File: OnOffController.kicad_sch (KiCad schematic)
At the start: 33 parts, among them J1 S2B-PH-K-SLFSN, J2 Conn_01x02_Pin, J3 Conn_01x04_Pin, J4 Conn_01x04_Pin, J8 47589-0001, SW1 KMR211GLFS, U1 STM6601, U2 MCP73831-2-OT, U3 SPX3819M5-L

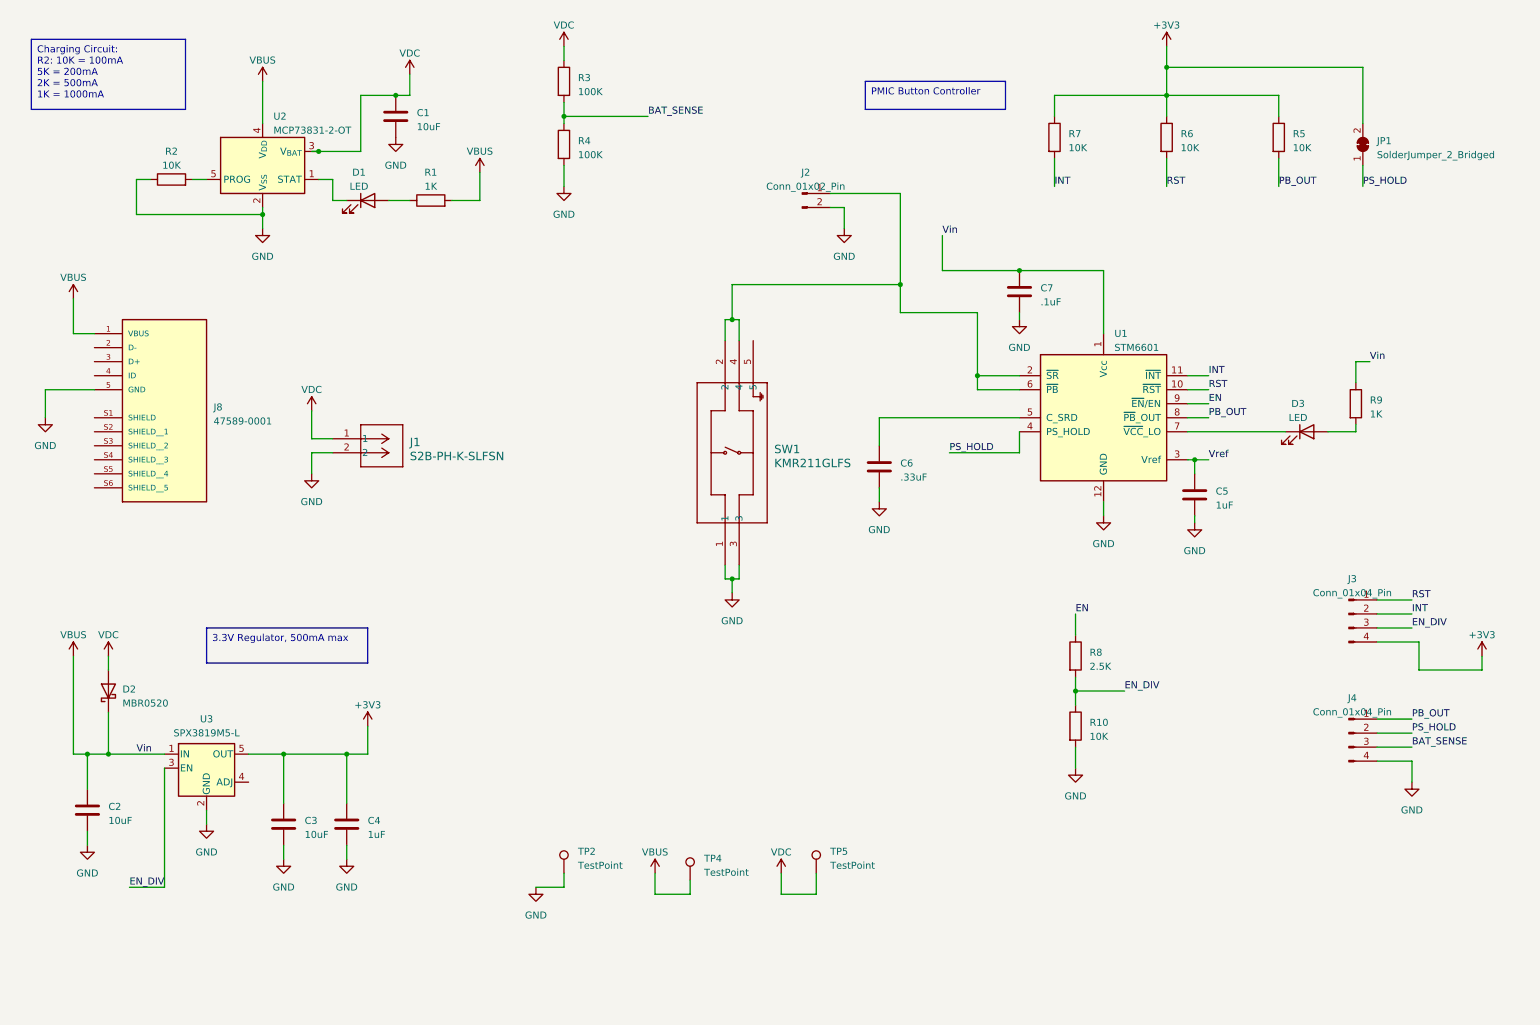
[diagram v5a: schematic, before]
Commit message: Updated all parts to smaller package sizes and found cheaper alternatives
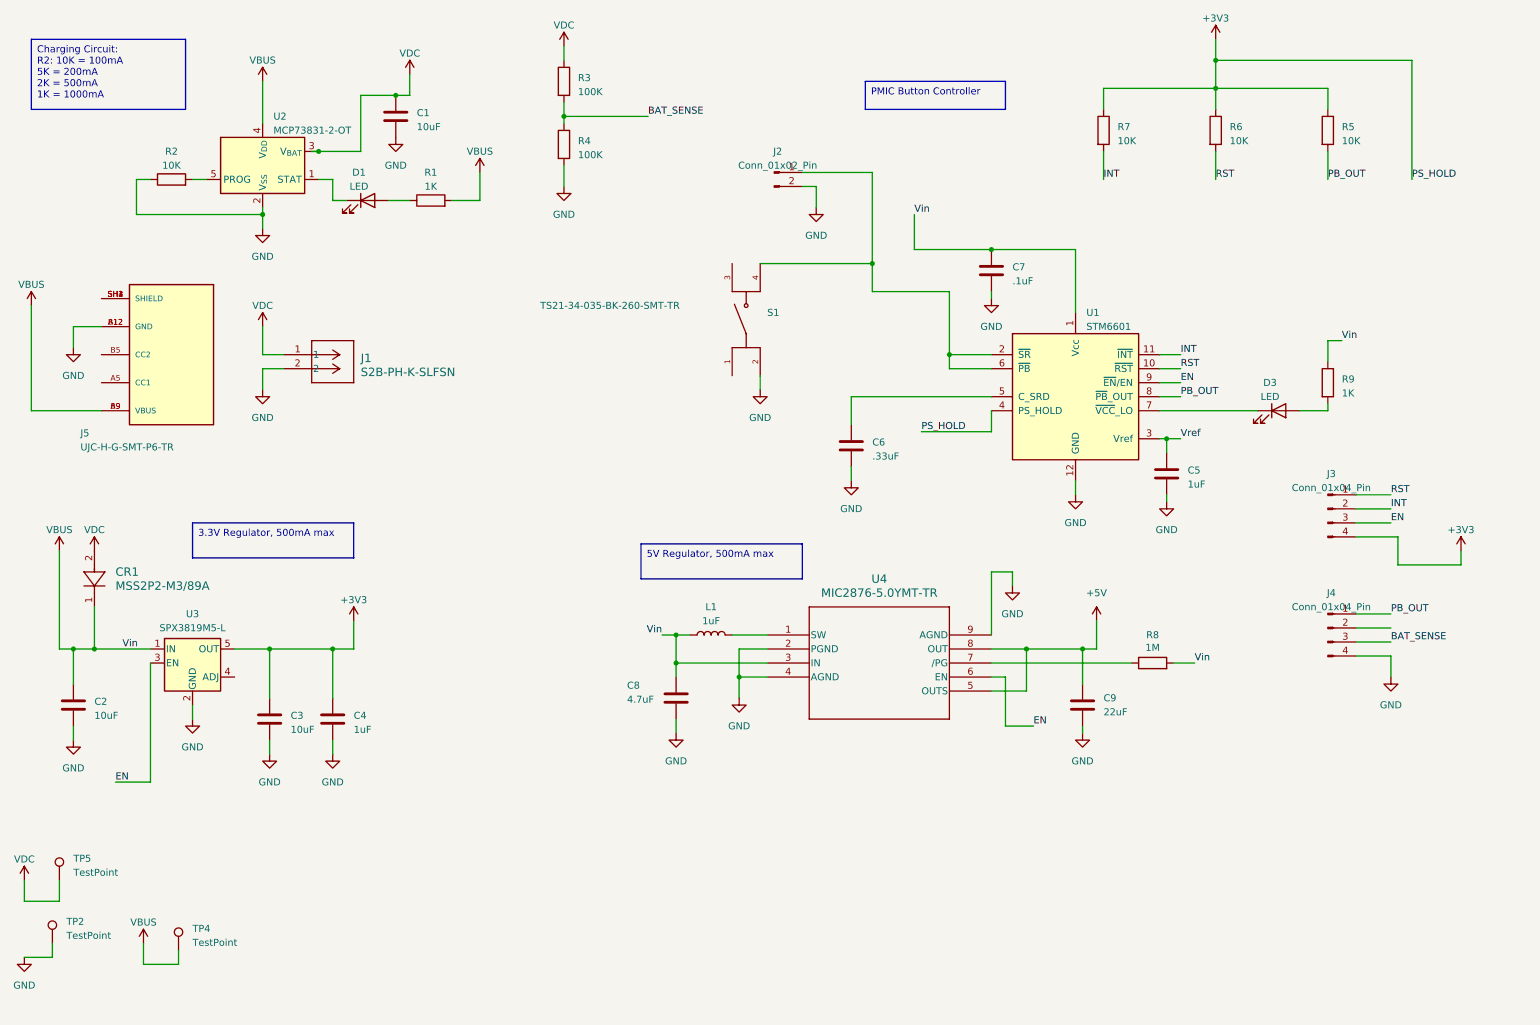
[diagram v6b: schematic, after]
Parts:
- removed D2: MBR0520, Diode_SMD:D_SOD-123, symbol Diode:MBR0520
- removed J8: 47589-0001, 47589_0001_USB_B:MOLEX_47589-0001, symbol 47589-0001_MOLEX_USB_B:47589-0001
- removed JP1: SolderJumper_2_Bridged, Jumper:SolderJumper-2_P1.3mm_Bridged_Pad1.0x1.5mm, symbol Jumper:SolderJumper_2_Bridged
- removed R10: 10K, Resistor_SMD:R_0603_1608Metric_Pad0.98x0.95mm_HandSolder, symbol Device:R
- removed SW1: KMR211GLFS, KMR2_Switch:KMR2xxG_CNK, symbol 2024-04-06_17-09-25_KMR_Switch:KMR211GLFS
- added C8: 4.7uF, Capacitor_SMD:C_0402_1005Metric, symbol Device:C
- added C9: 22uF, Capacitor_SMD:C_0603_1608Metric, symbol Device:C
- added CR1: MSS2P2-M3/89A, MSS2P2-M3:DIODE_MSP3V3, symbol MSS2P2-M3:MSS2P2-M3_89A
- added J5: UJC-H-G-SMT-P6-TR, UJC-H-G-SMT-P6-TR:SAMESKY_UJC-H-G-SMT-P6-TR, symbol UJC-H-G-SMT-P6-TR:UJC-H-G-SMT-P6-TR
- added L1: 1uF, Inductor_SMD:L_0805_2012Metric, symbol Device:L
- added S1: TS21-34-035-BK-260-SMT-TR, TS21-34-035-BK-260-SMT-TR:SW_TS21-34-035-BK-260-SMT-TR, symbol TS21_34_035_BK_260_SMT_TR:TS21-34-035-BK-260-SMT-TR
- added U4: MIC2876-5.0YMT-TR, MIC2876-5:UDFN8_2X2_MCH, symbol MIC2876-5:MIC2876-5.0YMT-TR
- C1, C2, C3, C4, C5, C6, C7: footprint Capacitor_SMD:C_0603_1608Metric_Pad1.08x0.95mm_HandSolder -> Capacitor_SMD:C_0402_1005Metric
- D1: footprint LED_SMD:LED_0805_2012Metric_Pad1.15x1.40mm_HandSolder -> LED_SMD:LED_0603_1608Metric
- D3: footprint LED_SMD:LED_0603_1608Metric_Pad1.05x0.95mm_HandSolder -> LED_SMD:LED_0603_1608Metric
- R1, R2, R3, R4, R5, R6, R7, R9: footprint Resistor_SMD:R_0603_1608Metric_Pad0.98x0.95mm_HandSolder -> Resistor_SMD:R_0402_1005Metric
- R8: value 2.5K -> 1M; footprint Resistor_SMD:R_0603_1608Metric_Pad0.98x0.95mm_HandSolder -> Resistor_SMD:R_0402_1005Metric
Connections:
- net +3V3: now also U1.4 (PS_HOLD)
- net EN: now also J3.3 (Pin_3), U3.3 (EN), U4.6 (EN); no longer R8.1
- net GND: now also C8.2, C9.2, J5.A12 (GND), J5.B12 (GND), S1.2, U4.2 (PGND), U4.4 (AGND), U4.9 (AGND)
- net VBUS: now also R8.2, C8.1, CR1.1, J5.A9 (VBUS), J5.B9 (VBUS), L1.1, U4.3 (IN)
- net VDC: now also CR1.2
- net at J2.1 (Pin_1), U1.2 (~{SR}), U1.6 (~{PB}): now also S1.4
- removed net EN_DIV: J3.3 (Pin_3), R8.2, U3.3 (EN)
- net PS_HOLD: no longer names the net of J4.2 (Pin_2)
- net PS_HOLD: no longer U1.4 (PS_HOLD)
- new net: L1.2, U4.1 (SW)
- new net: R8.1, U4.7 (/PG)
- new net: J5.SH1 (SHIELD), J5.SH2 (SHIELD), J5.SH3 (SHIELD), J5.SH4 (SHIELD)
- new net +5V: C9.1, U4.5 (OUTS), U4.8 (OUT)
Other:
- moved on the sheet: C2, C3, C4, C5, C6, C7, D3, J1, J2, J3, J4, R5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

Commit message: Updated to 5V and 3.3V versions
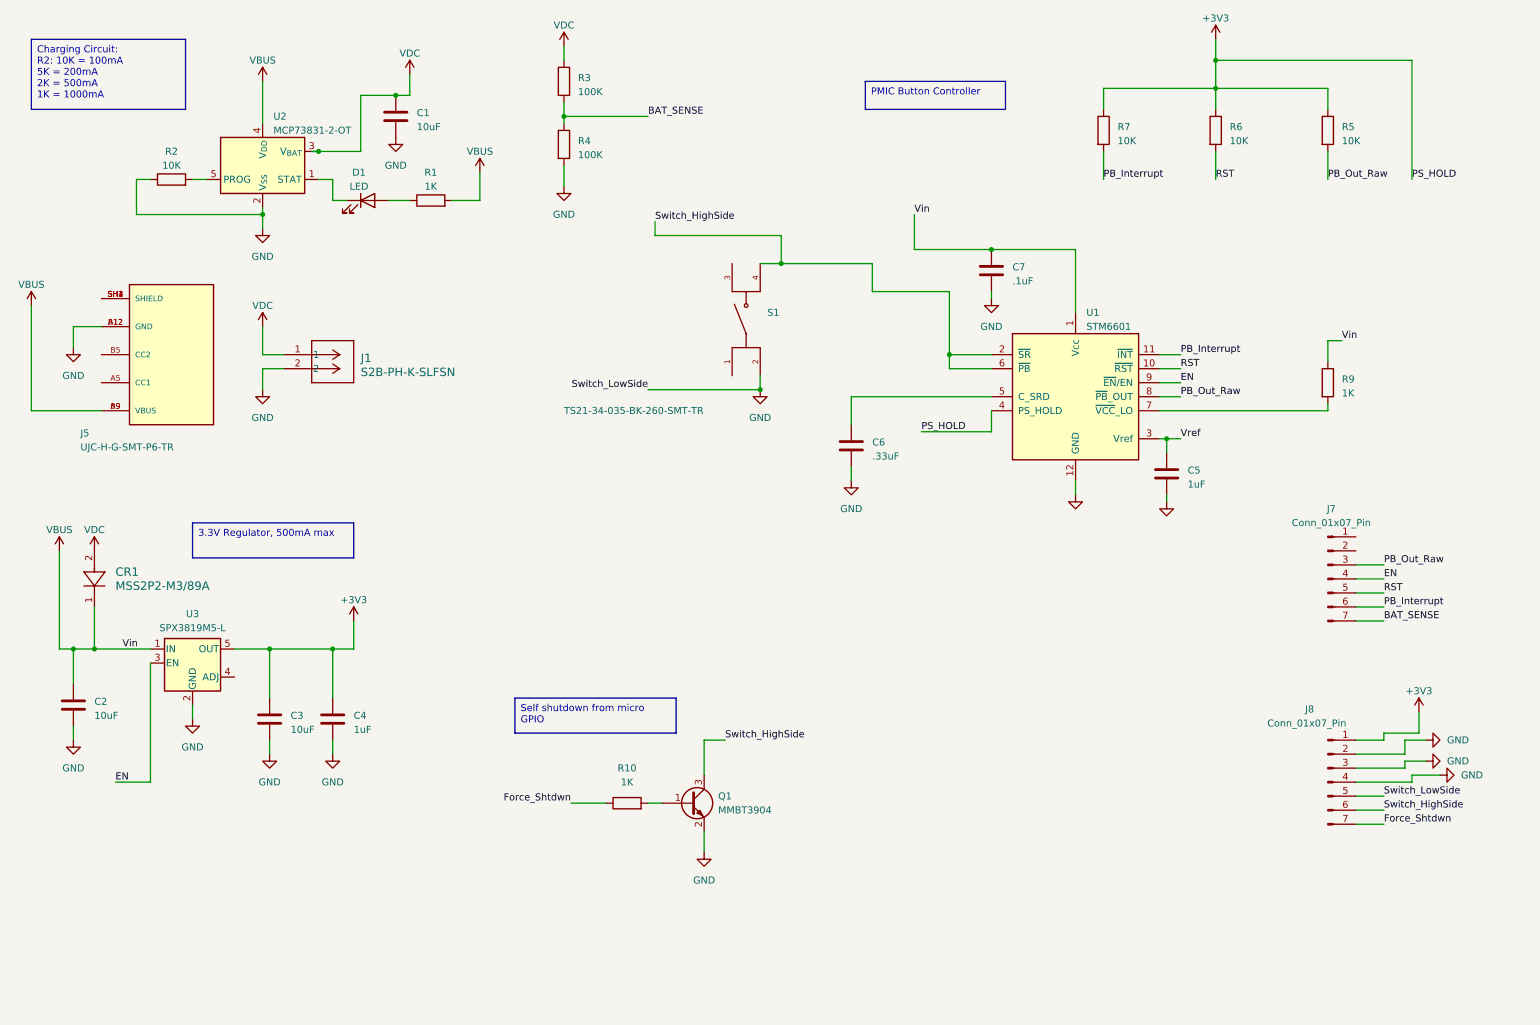
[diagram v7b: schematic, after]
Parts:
- removed C8: 4.7uF, Capacitor_SMD:C_0402_1005Metric, symbol Device:C
- removed C9: 22uF, Capacitor_SMD:C_0603_1608Metric, symbol Device:C
- removed D3: LED, LED_SMD:LED_0603_1608Metric, symbol Device:LED
- removed J2: Conn_01x02_Pin, Connector_PinHeader_2.54mm:PinHeader_1x02_P2.54mm_Vertical, symbol Connector:Conn_01x02_Pin
- removed J3, J4: Conn_01x04_Pin, Connector_PinHeader_2.54mm:PinHeader_1x04_P2.54mm_Vertical, symbol Connector:Conn_01x04_Pin
- removed L1: 1uF, Inductor_SMD:L_0805_2012Metric, symbol Device:L
- removed R8: 1M, Resistor_SMD:R_0402_1005Metric, symbol Device:R
- removed TP2, TP4, TP5: TestPoint, TestPoint:TestPoint_Pad_D1.5mm, symbol Connector:TestPoint
- removed U4: MIC2876-5.0YMT-TR, MIC2876-5:UDFN8_2X2_MCH, symbol MIC2876-5:MIC2876-5.0YMT-TR
- added J7, J8: Conn_01x07_Pin, Connector_PinHeader_2.54mm:qtpy_catellated_7x2, symbol Connector:Conn_01x07_Pin
- added Q1: MMBT3904, Package_TO_SOT_SMD:SOT-23, symbol Transistor_BJT:MMBT3904
- added R10: 1K, Resistor_SMD:R_0402_1005Metric, symbol Device:R
- S1: footprint TS21-34-035-BK-260-SMT-TR:SW_TS21-34-035-BK-260-SMT-TR -> TS21_34_035_BK_260:SW_TS21-34-035-BK-260-SMT-TR
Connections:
- net +3V3: now also J8.1 (Pin_1)
- net BAT_SENSE: now also J7.7 (Pin_7)
- net EN: now also J7.4 (Pin_4)
- net GND: now also J8.2 (Pin_2), J8.3 (Pin_3), J8.4 (Pin_4), J8.5 (Pin_5), Q1.2 (E)
- net RST: now also J7.5 (Pin_5)
- net at R9.2: now also U1.7 (~{VCC}_LO)
- net Switch_HighSide: now reaches S1.4, U1.2 (~{SR}), U1.6 (~{PB})
- net Switch_HighSide: now also J8.6 (Pin_6), Q1.3 (C)
- net INT renamed PB_Interrupt
- net PB_Interrupt: now also J7.6 (Pin_6)
- net PB_OUT renamed PB_Out_Raw
- net PB_Out_Raw: now also J7.3 (Pin_3)
- new net: Q1.1 (B), R10.2
- new net Force_Shtdwn: J8.7 (Pin_7), R10.1
